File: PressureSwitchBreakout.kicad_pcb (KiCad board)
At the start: 2 copper layers, 15.2 x 23.4 mm, 8 parts, among them J1 TEST

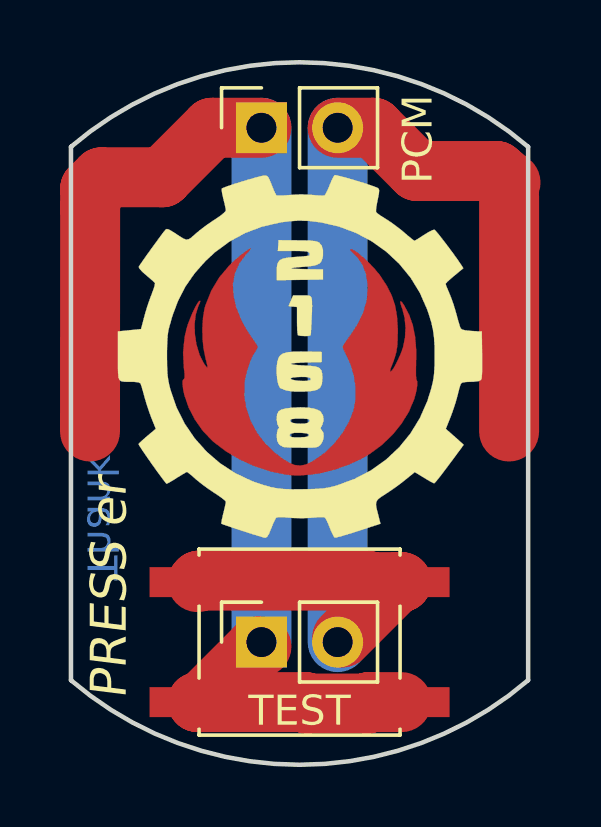
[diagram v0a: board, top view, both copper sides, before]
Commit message: Update to kicad 6.0 export gerbers panelize using kikit
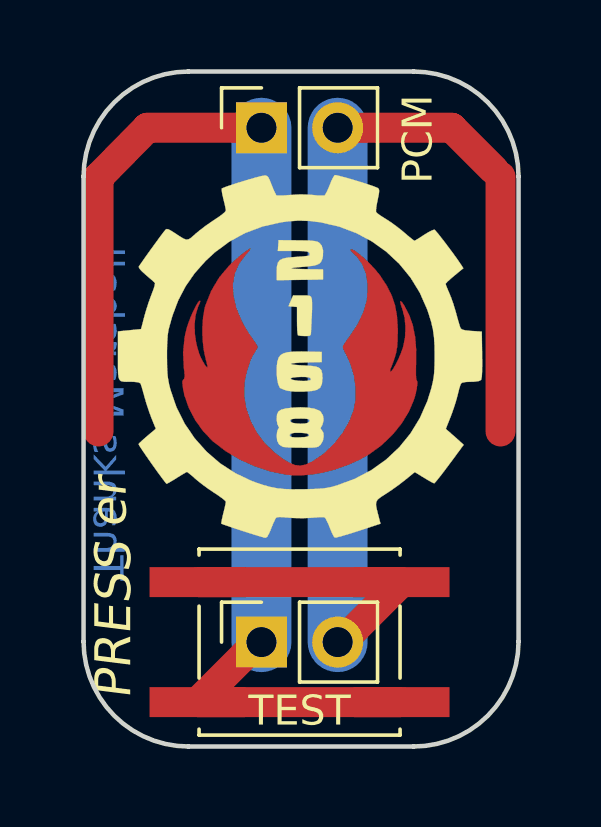
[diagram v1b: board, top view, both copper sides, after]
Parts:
- added REF**: Tab, kikit:Tab, F.Cu at (139.8, 77.1)
- added REF**: Tab, kikit:Tab, F.Cu at (139.8, 100.3)
- added REF**: Tab, kikit:Tab, F.Cu at (132.1, 95.0)
- added REF**: Tab, kikit:Tab, F.Cu at (132.1, 82.5)
- added REF**: Tab, kikit:Tab, F.Cu at (147.4, 95.0)
- added REF**: Tab, kikit:Tab, F.Cu at (147.4, 82.5)
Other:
- board size 15.2 x 23.4 mm -> 14.5 x 22.5 mm
- net class Default removed
- rule pad_to_mask_clearance: 0.051 -> 0
- board text added: "211228.01"
- board text removed: "190122.01"
